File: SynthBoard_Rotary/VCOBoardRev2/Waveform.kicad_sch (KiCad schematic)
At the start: 24 parts, among them IC3 AS321KTR-E1, IC4 4013, Q1 2SC3325-Y

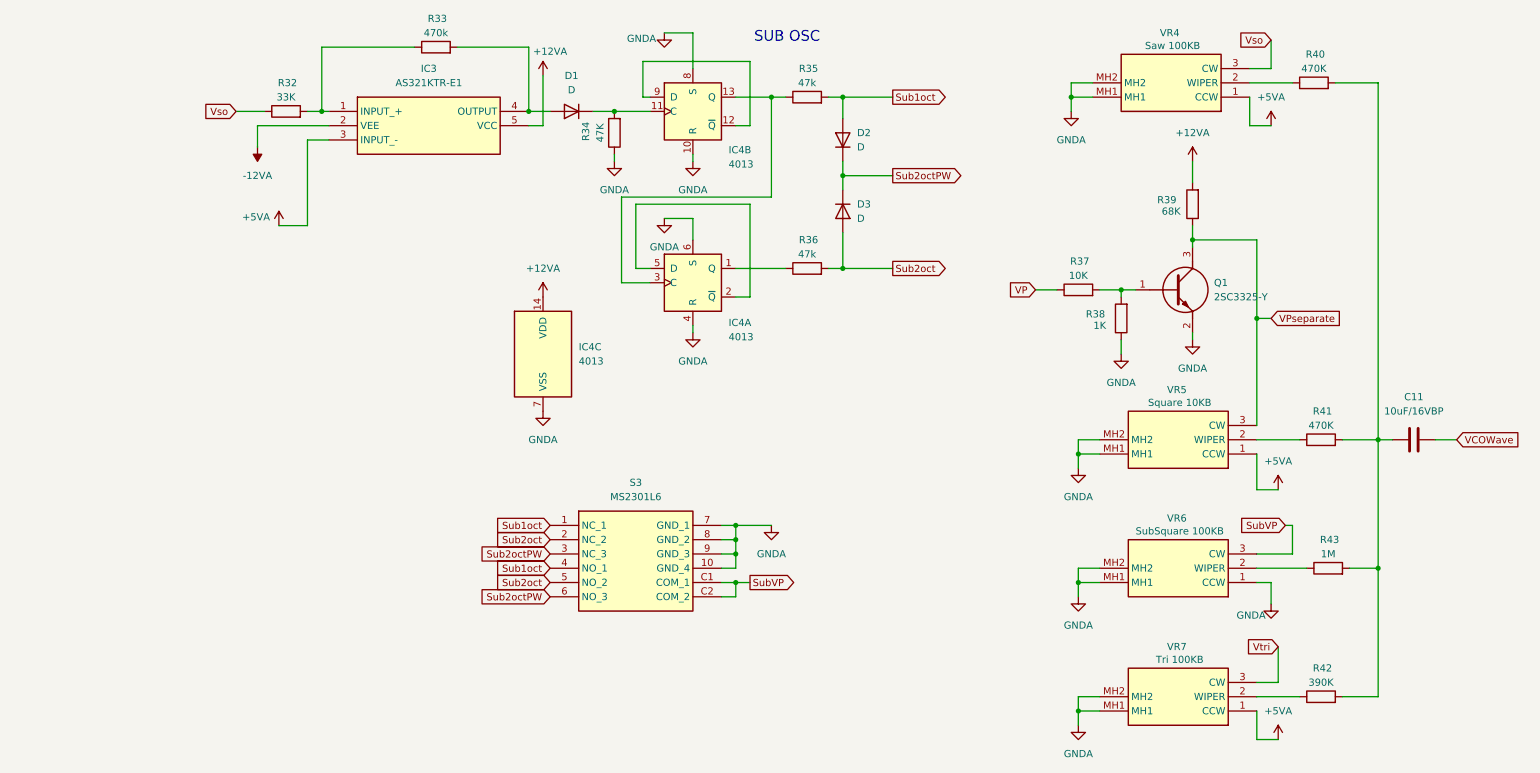
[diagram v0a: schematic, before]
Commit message: MC2 Synth-Board Rotary
V0.2
U10:PIn4 -12Vに接続
IC4:Pin12,13 デフォルト12でジャンパーパッドを追加
R86:三角波をS2に未接続だったのを修正
S2,S3:スイッチ動作を上下入れ替え
VR9:右に2.5mm移動に伴い周辺回路の配置を変更
冗長な配線を修正
ビアを打った
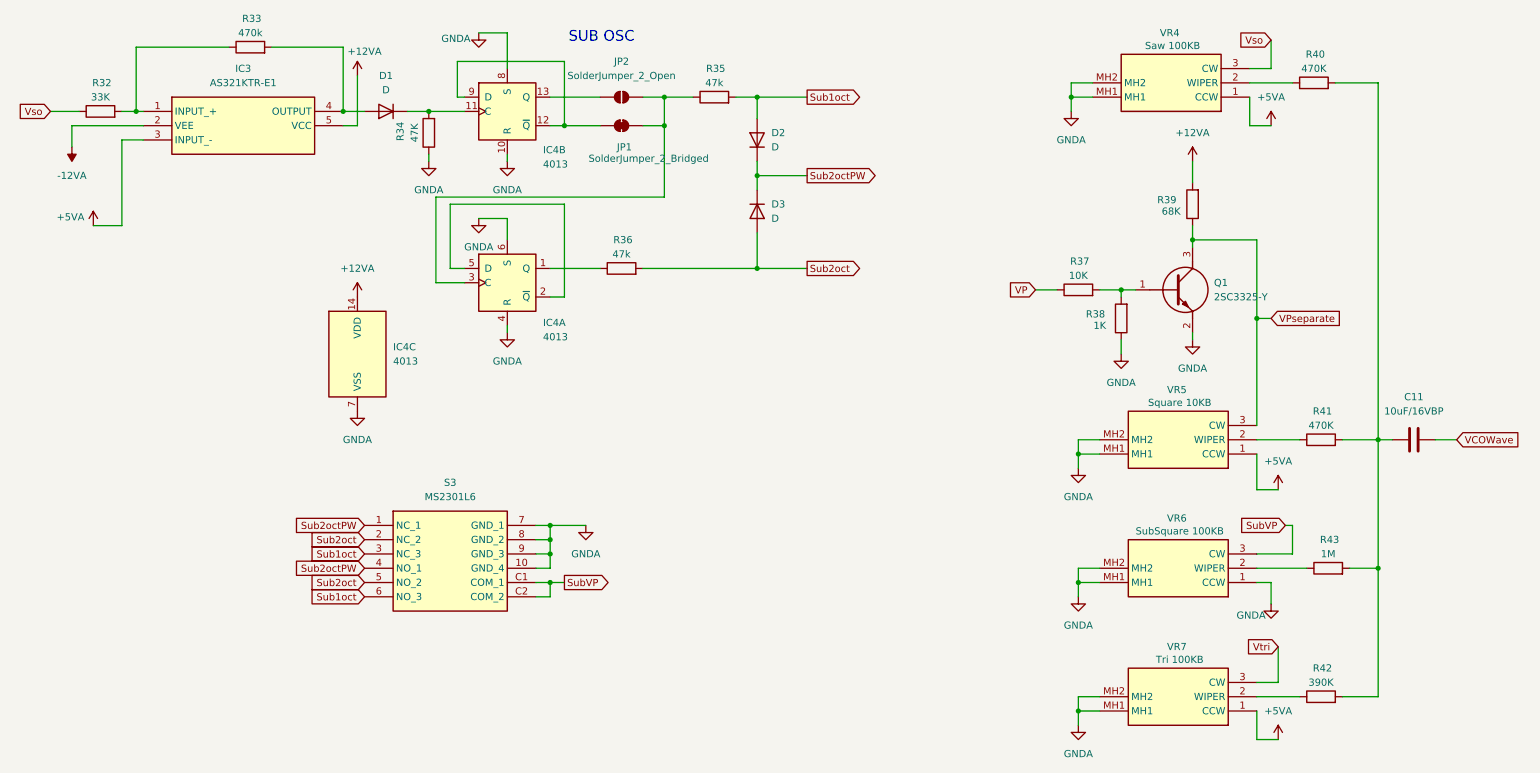
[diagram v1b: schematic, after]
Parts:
- added JP1: SolderJumper_2_Bridged, Jumper:SolderJumper-2_P1.3mm_Bridged2Bar_RoundedPad1.0x1.5mm, symbol Jumper:SolderJumper_2_Bridged
- added JP2: SolderJumper_2_Open, Jumper:SolderJumper-2_P1.3mm_Open_RoundedPad1.0x1.5mm, symbol Jumper:SolderJumper_2_Open
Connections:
- net Sub1oct: now also S3.3 (NC_3), S3.6 (NO_3); no longer S3.1 (NC_1), S3.4 (NO_1)
- net Sub2octPW: now also S3.1 (NC_1), S3.4 (NO_1); no longer S3.3 (NC_3), S3.6 (NO_3)
- net at IC4.12 (~{Q}), IC4.9 (D): now also JP1.1 (A)
- net at IC4.3 (C), R35.1: now also JP1.2 (B), JP2.2 (B); no longer IC4.13 (Q)
- new net: IC4.13 (Q), JP2.1 (A)
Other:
- moved on the sheet: D1, D2, D3, IC3, IC4A, IC4B, IC4C, R32, R33, R34, R35, R36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
